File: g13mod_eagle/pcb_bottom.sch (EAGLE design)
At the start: 8 parts

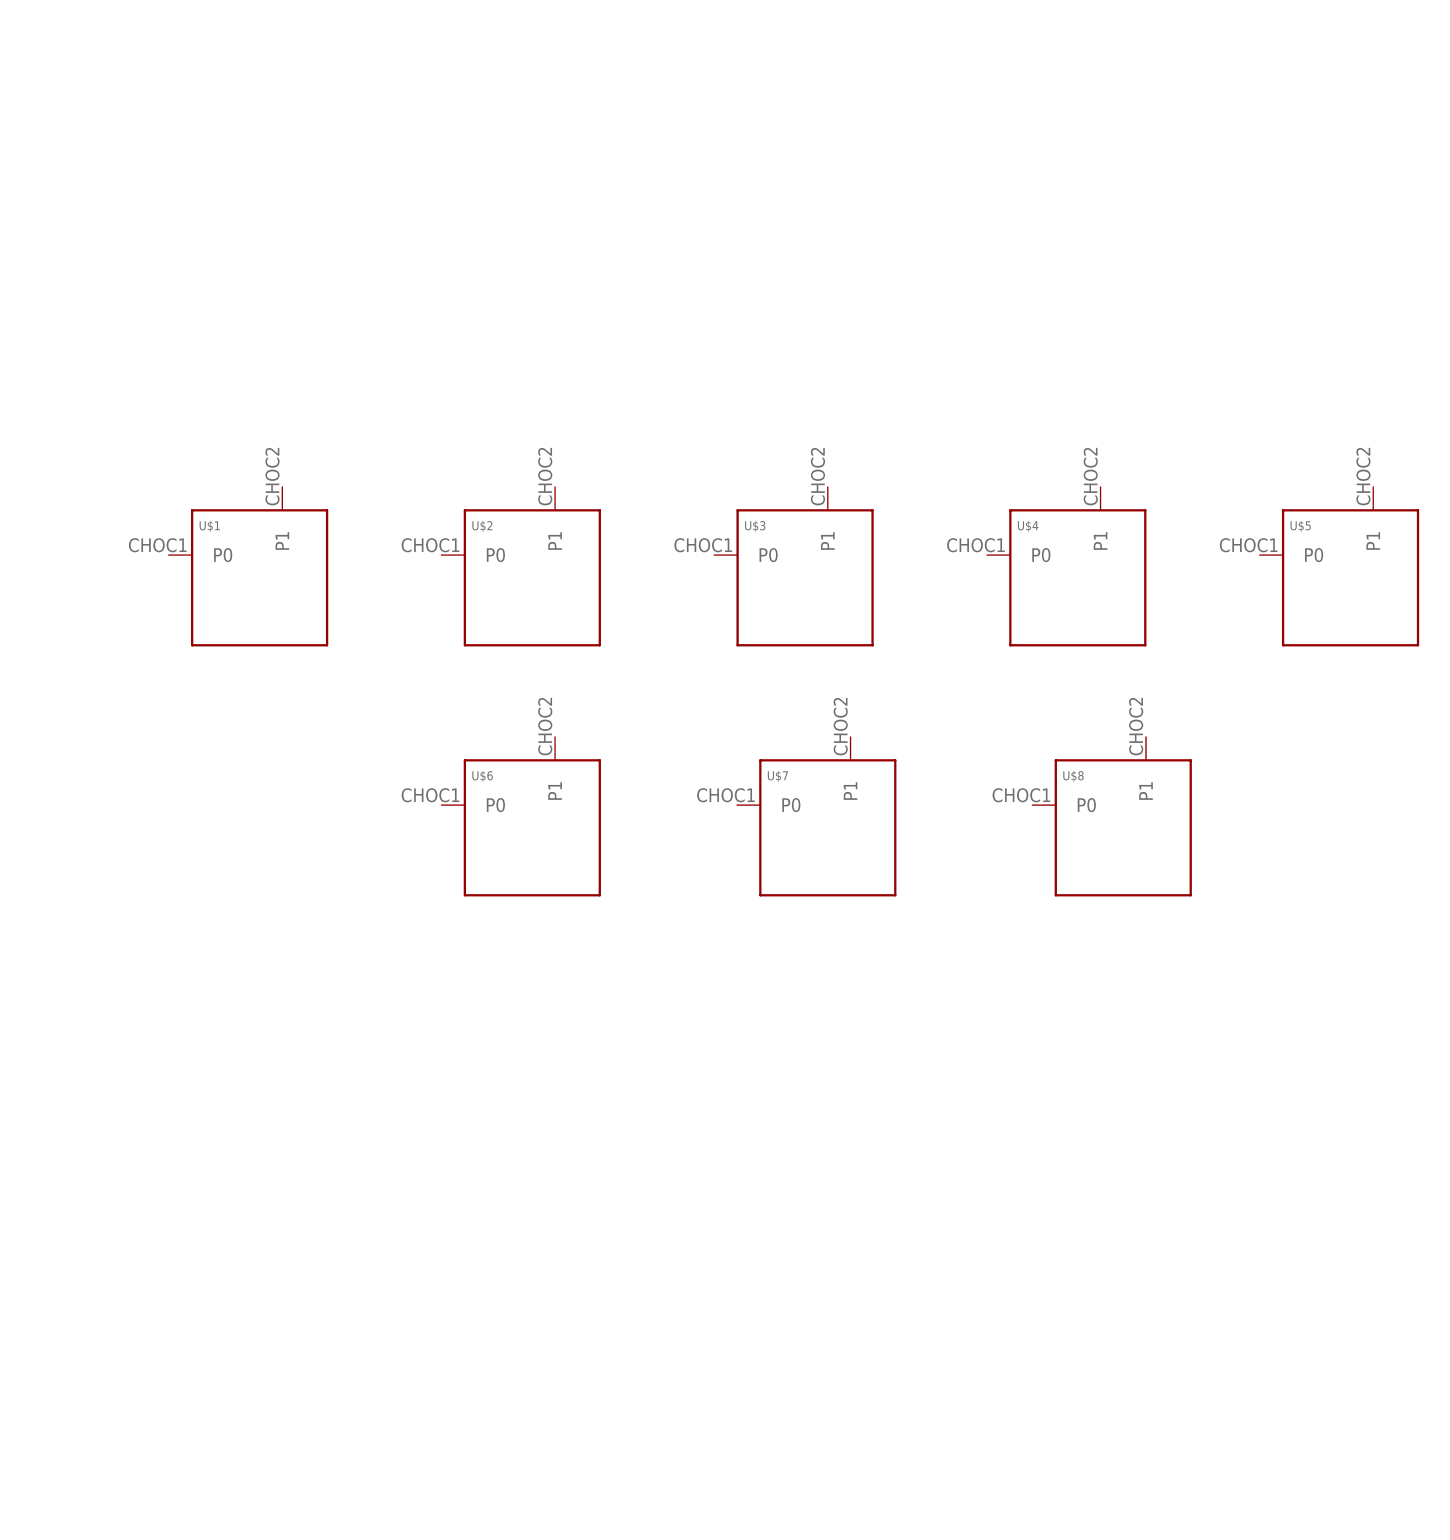
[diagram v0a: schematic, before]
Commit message: wiring bottom pcb
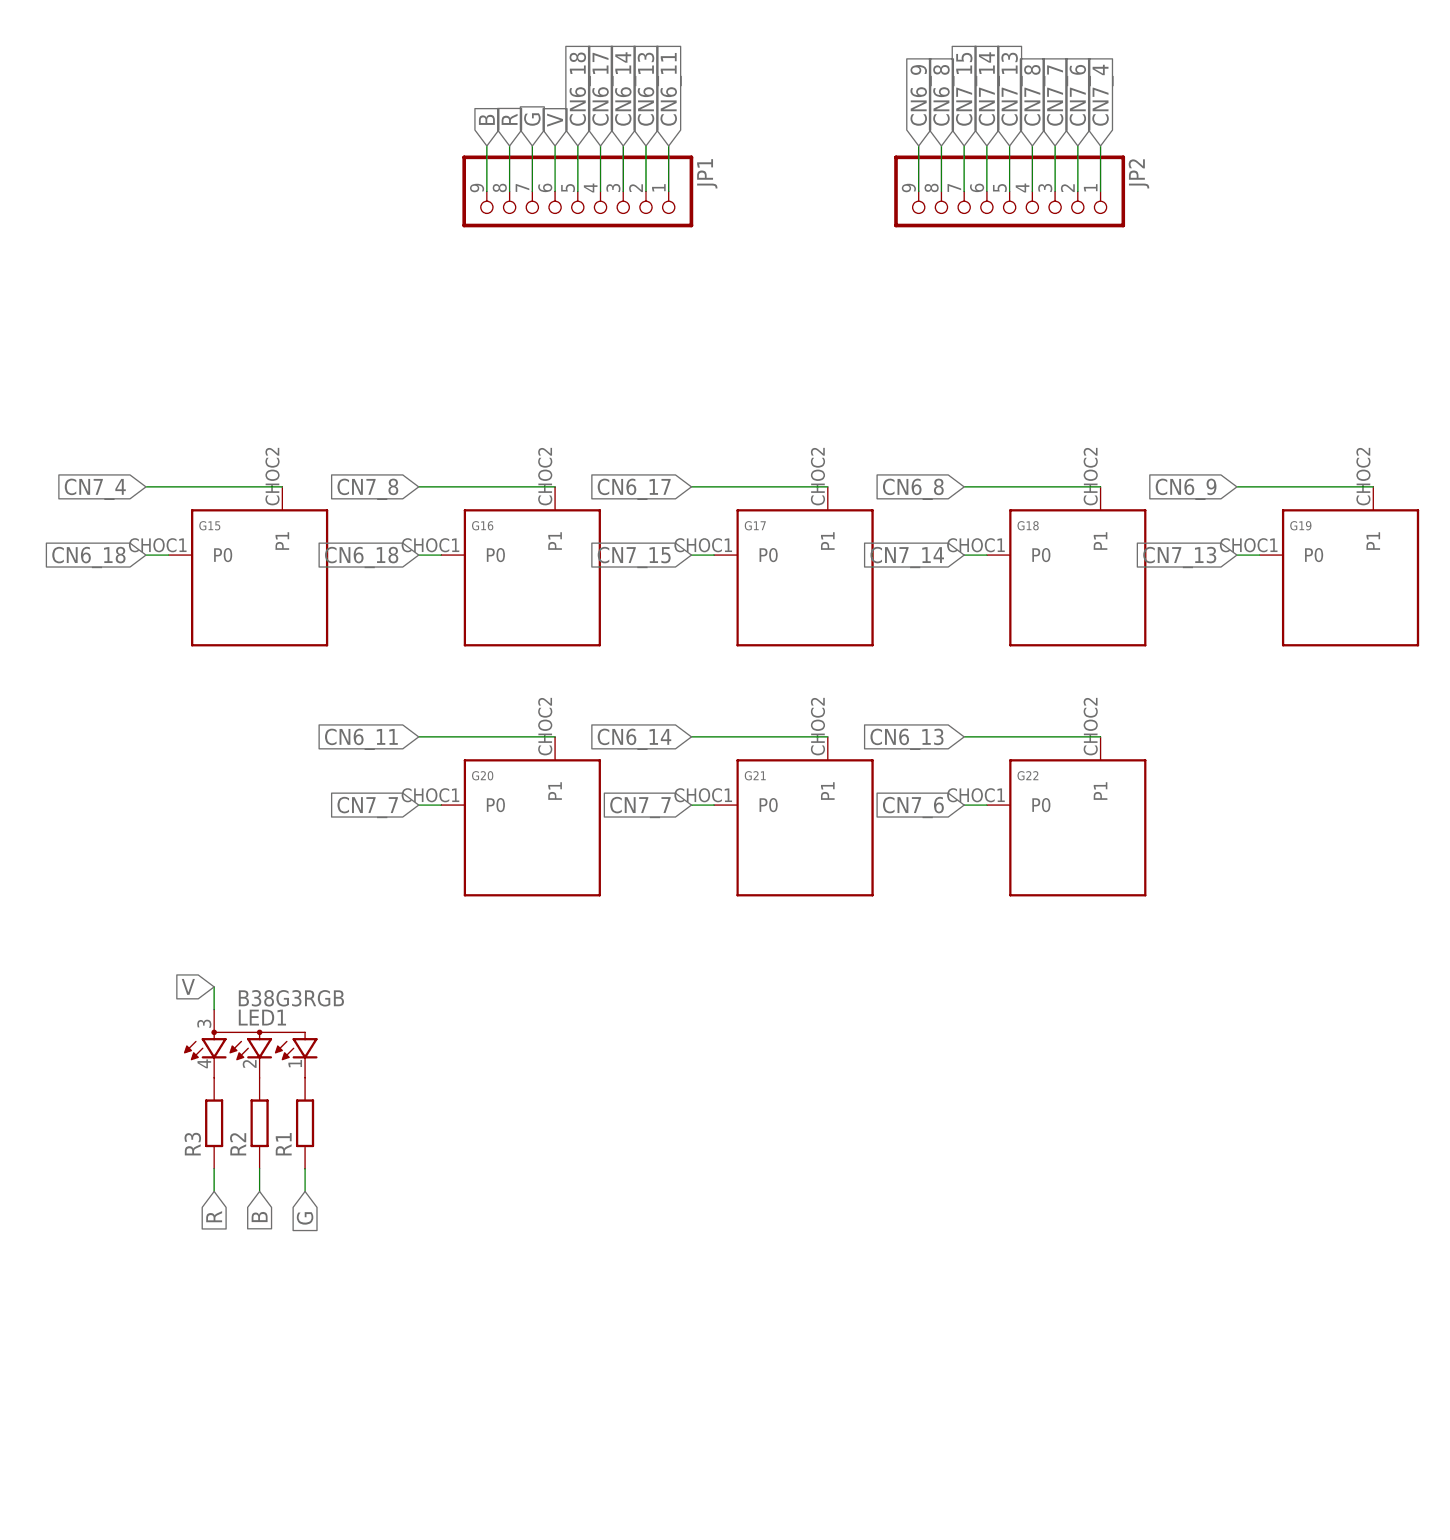
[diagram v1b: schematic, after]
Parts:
- removed U$7, U$8: KEYSWITCH-PLAIN-CHOC-1U, Keyboard:KEYSWITCH-PLAIN-CHOC-1U
- added G21, G22: KEYSWITCH-PLAIN-CHOC-1U, Keyboard:KEYSWITCH-PLAIN-CHOC-1U
- added JP1, JP2: (no value), pinhead-half-pitch:THROUHOLE09
- added LED1: B38G3RGB, led_rgb:B38G3RGB
- added R1, R2, R3: (no value), rcl:R-EU_R0603
- renumbered U$1 to G15, U$2 to G16, U$3 to G17, U$4 to G18, U$5 to G19, U$6 to G20
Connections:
- new net B: JP1.9, R2.1
- new net CN6_11: G20.P1, JP1.1
- new net CN6_13: G22.P1, JP1.2
- new net CN6_14: G21.P1, JP1.3
- new net CN6_17: G17.P1, JP1.4
- new net CN6_18: G15.P0, G16.P0, JP1.5
- new net CN6_8: G18.P1, JP2.8
- new net CN6_9: G19.P1, JP2.9
- new net CN7_13: G19.P0, JP2.5
- new net CN7_14: G18.P0, JP2.6
- new net CN7_15: G17.P0, JP2.7
- new net CN7_4: G15.P1, JP2.1
- new net CN7_6: G22.P0, JP2.2
- new net CN7_7: G20.P0, G21.P0, JP2.3
- new net CN7_8: G16.P1, JP2.4
- new net G: JP1.7, R1.1
- new net N$1: LED1.CGREEN, R1.2
- new net N$2: LED1.CBLUE, R2.2
- new net N$3: LED1.CRED, R3.2
- new net R: JP1.8, R3.1
- new net V: JP1.6, LED1.A

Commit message: wiring bottom pcb
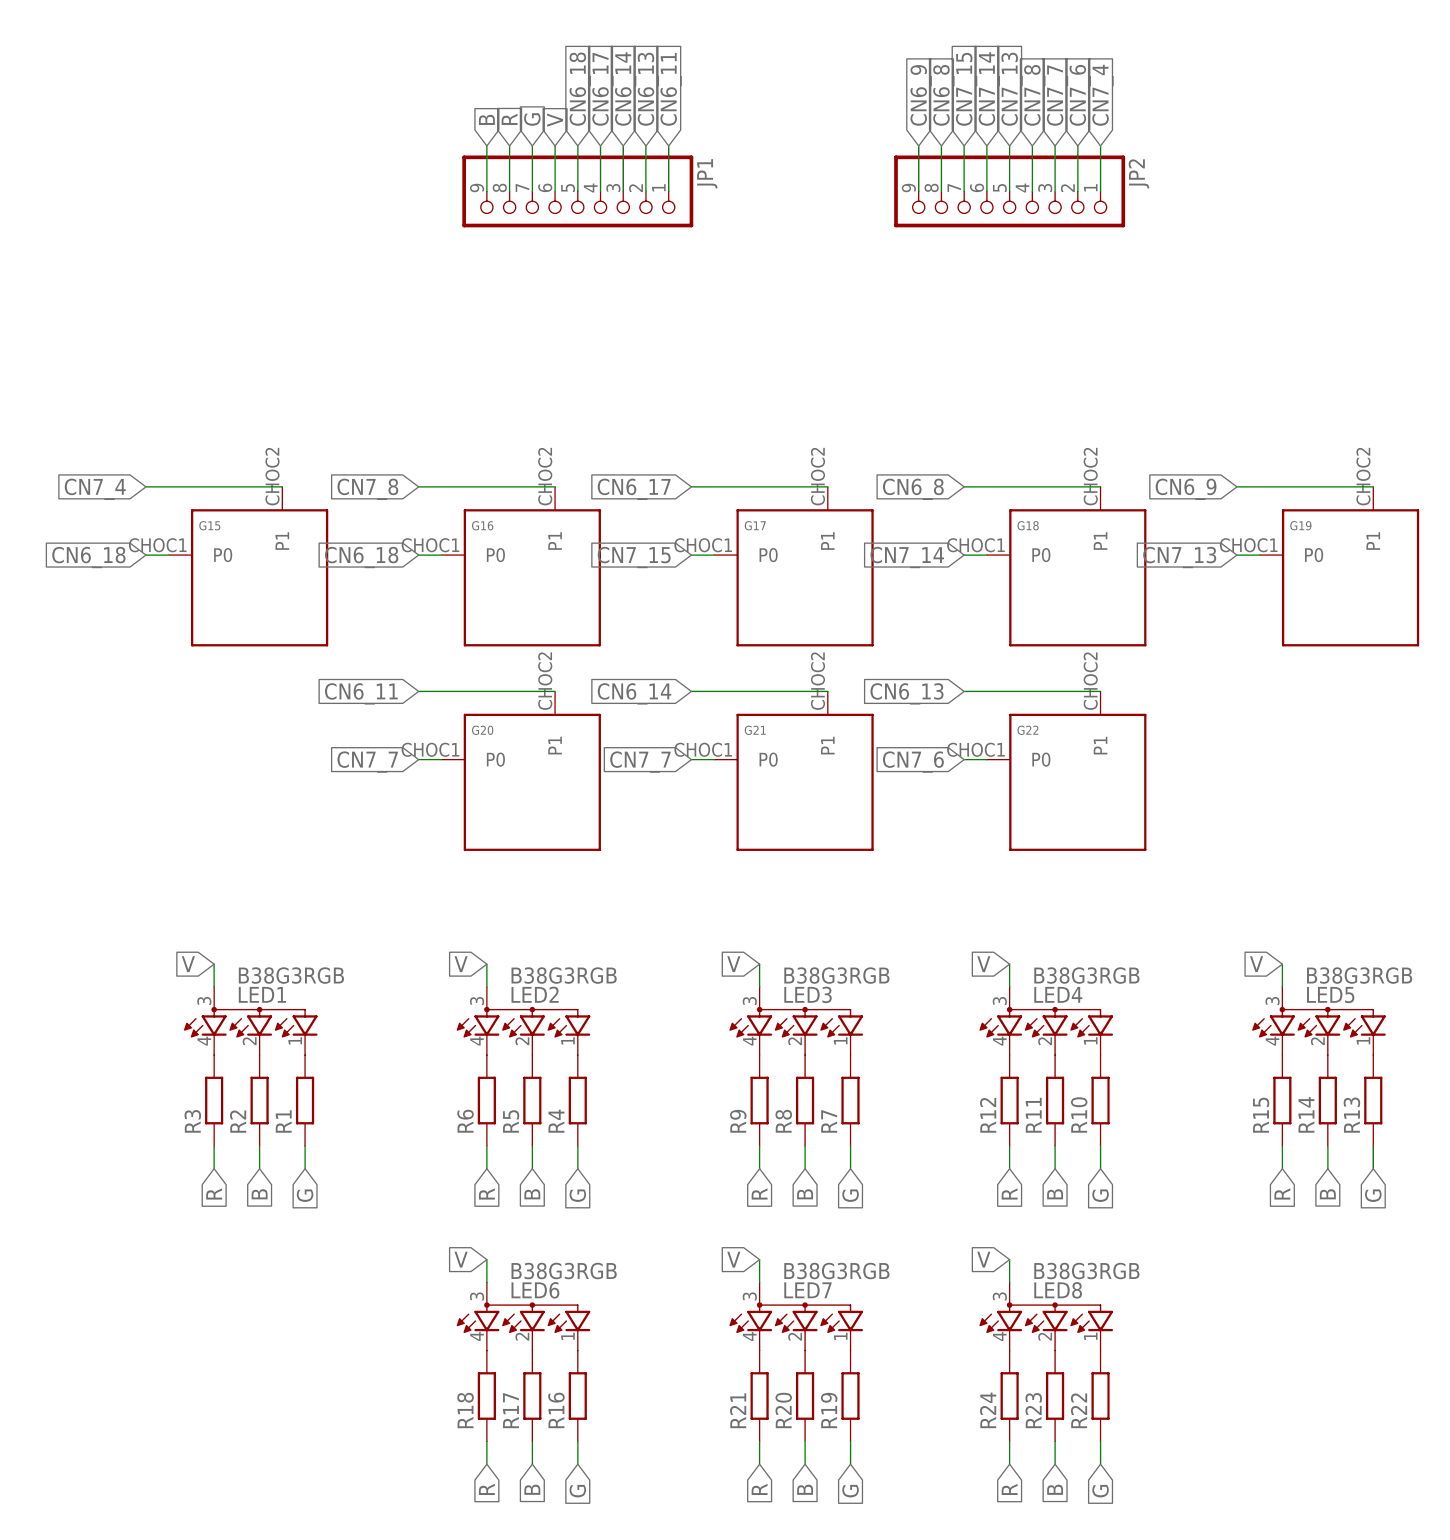
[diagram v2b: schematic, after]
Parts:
- added LED2, LED3, LED4, LED5, LED6, LED7, LED8: B38G3RGB, led_rgb:B38G3RGB
- added R10, R11, R12, R13, R14, R15, R16, R17, R18, R19, R20, R21, R22, R23, R24, R4, R5, R6, R7, R8, R9: (no value), rcl:R-EU_R0603
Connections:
- new net N$10: LED4.CGREEN, R10.2
- new net N$11: LED4.CBLUE, R11.2
- new net N$12: LED4.CRED, R12.2
- new net N$13: LED5.CGREEN, R13.2
- new net N$14: LED5.CBLUE, R14.2
- new net N$15: LED5.CRED, R15.2
- new net N$16: LED6.CGREEN, R16.2
- new net N$17: LED6.CBLUE, R17.2
- new net N$18: LED6.CRED, R18.2
- new net N$19: LED7.CGREEN, R19.2
- new net N$20: LED7.CBLUE, R20.2
- new net N$21: LED7.CRED, R21.2
- new net N$22: LED8.CGREEN, R22.2
- new net N$23: LED8.CBLUE, R23.2
- new net N$24: LED8.CRED, R24.2
- new net N$4: LED2.CGREEN, R4.2
- new net N$5: LED2.CBLUE, R5.2
- new net N$6: LED2.CRED, R6.2
- new net N$7: LED3.CGREEN, R7.2
- new net N$8: LED3.CBLUE, R8.2
- new net N$9: LED3.CRED, R9.2
- net B: now also R11.1, R14.1, R17.1, R20.1, R23.1, R5.1, R8.1
- net G: now also R10.1, R13.1, R16.1, R19.1, R22.1, R4.1, R7.1
- net R: now also R12.1, R15.1, R18.1, R21.1, R24.1, R6.1, R9.1
- net V: now also LED2.A, LED3.A, LED4.A, LED5.A, LED6.A, LED7.A, LED8.A
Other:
- moved on the sheet: G20, G21, G22, LED1, R1, R2, R3
